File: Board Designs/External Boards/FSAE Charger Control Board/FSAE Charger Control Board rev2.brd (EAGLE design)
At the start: 67.8 x 86.5 mm, 38 parts, among them X1 CONNECTOR-4, X2 CONNECTOR-12

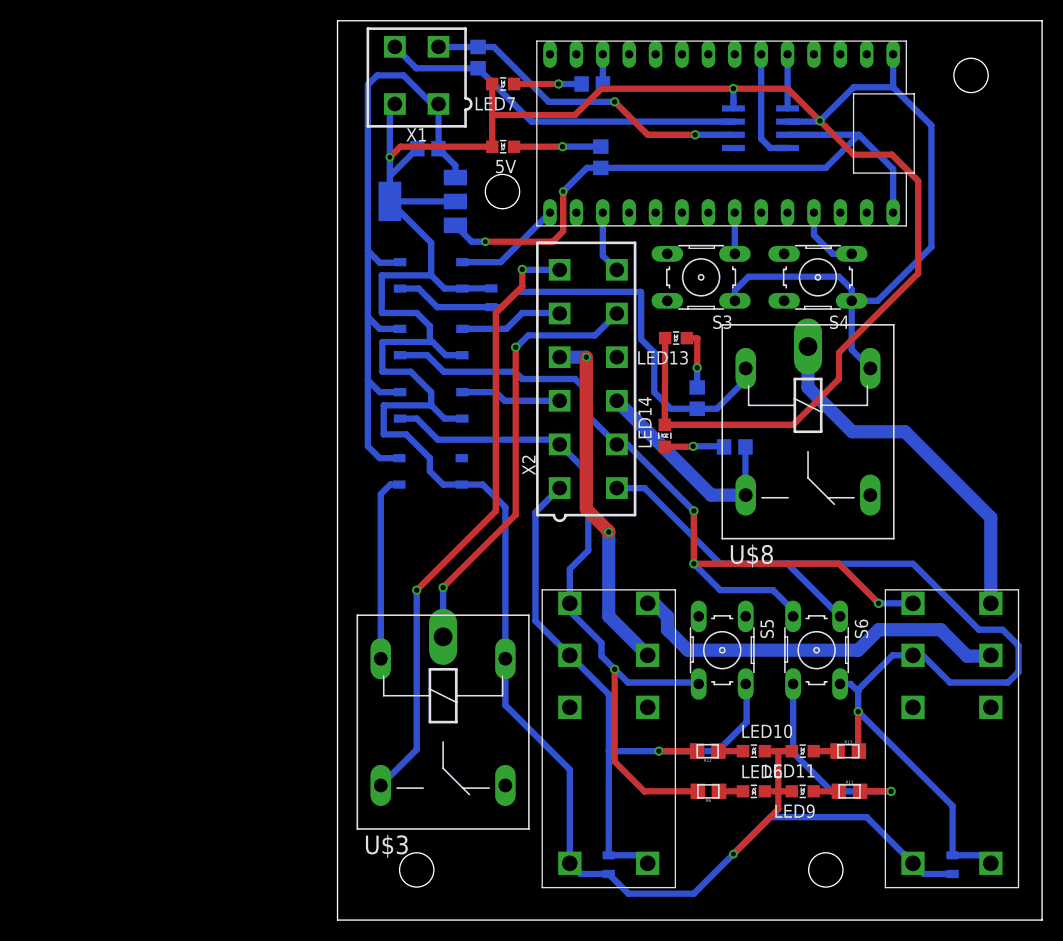
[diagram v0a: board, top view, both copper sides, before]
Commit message: Revising schematics for FSAE ESF
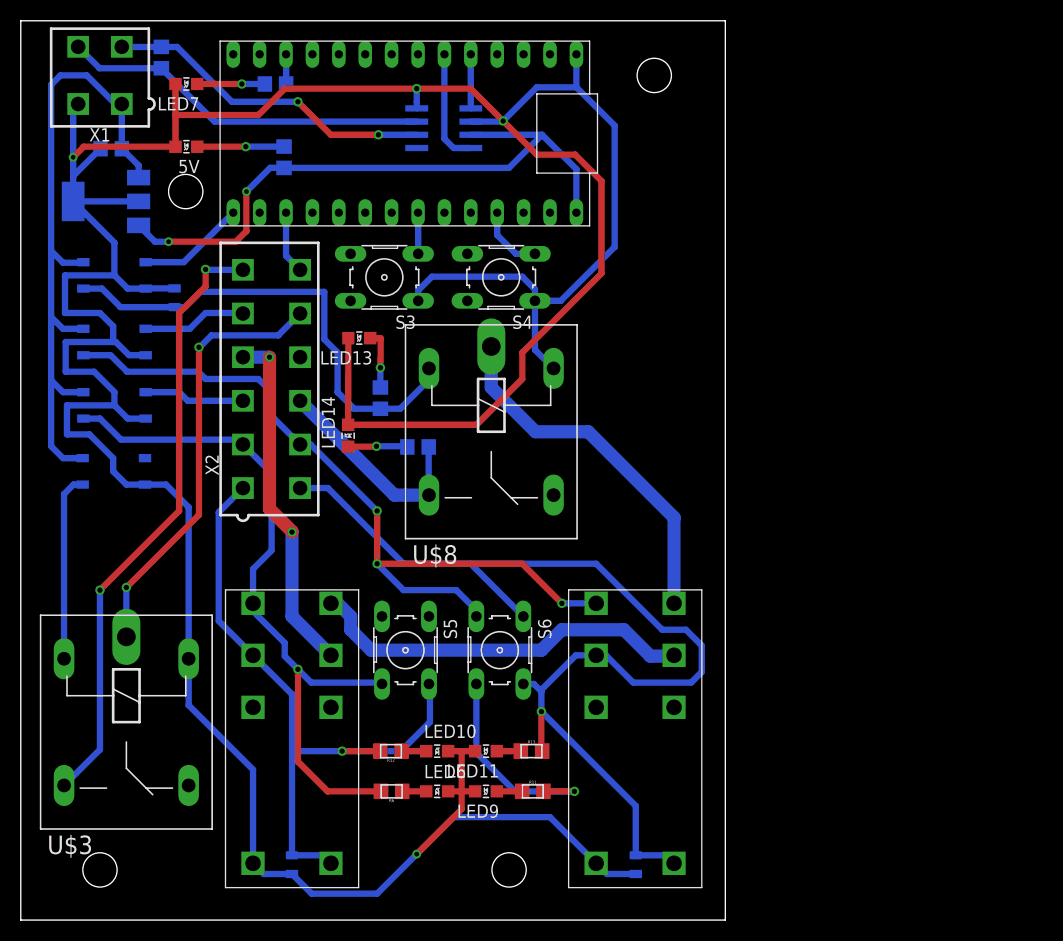
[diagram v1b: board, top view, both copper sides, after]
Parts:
- moved 5V 30.5 mm to (15.9, 74.4)
- moved 5VREG 30.5 mm to (8.19, 69.2)
- moved D5 30.5 mm to (59.2, 5.33)
- moved LED10 30.5 mm to (40.1, 16.3)
- moved LED11 30.5 mm to (44.8, 16.3)
- moved LED13 30.5 mm to (32.6, 56.0)
- moved LED6 30.5 mm to (40.1, 12.4)
- moved LED7 30.5 mm to (15.9, 80.5)
- moved LED9 30.5 mm to (44.8, 12.4)
- moved R13 30.5 mm to (49.1, 16.3)
- moved R15 30.5 mm to (34.6, 50.2)
- moved R6 30.5 mm to (35.7, 12.4)
- moved S3 30.5 mm to (35.0, 61.8)
- moved S5 30.5 mm to (37.0, 26.0)
- moved S6 30.5 mm to (46.1, 26.0)
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
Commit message: Added resistors to SSRs
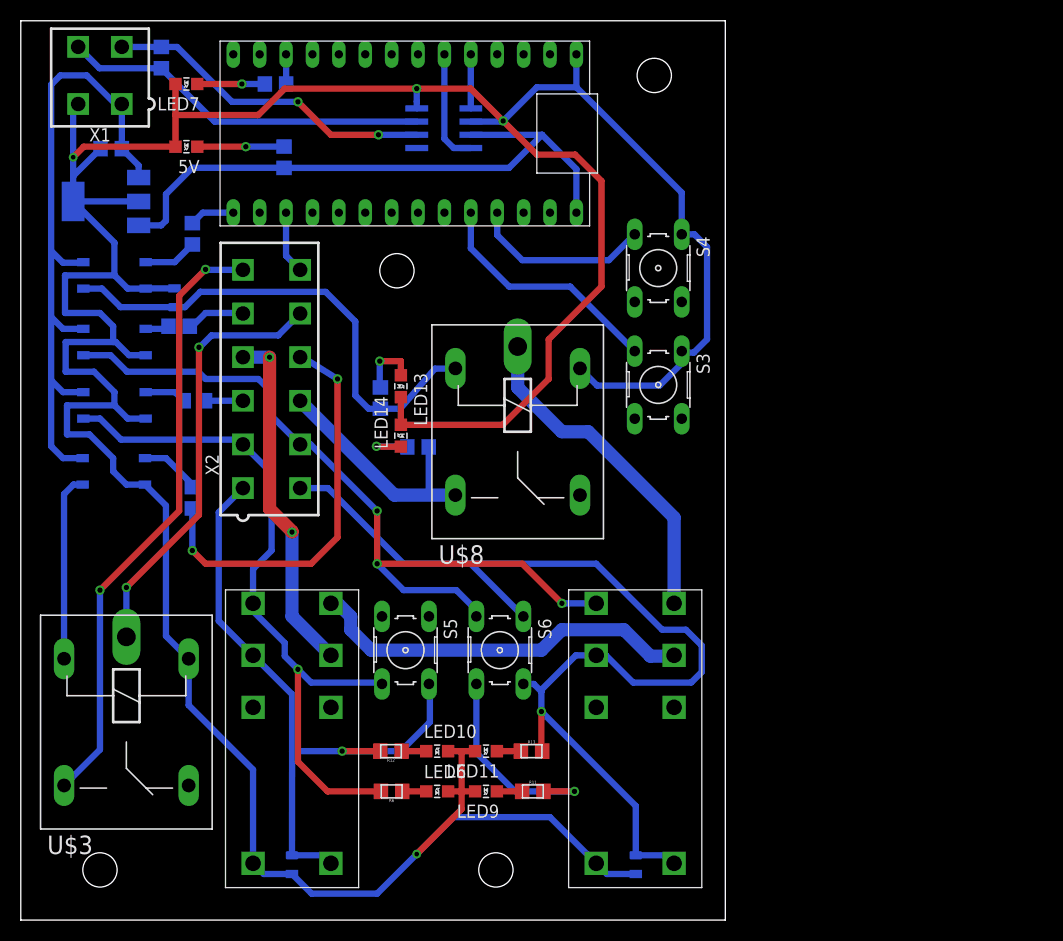
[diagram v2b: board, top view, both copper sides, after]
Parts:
- added R2, R3, R4, R5: (no value), HyTechDevices:0805
- moved S3 28.3 mm to (61.3, 51.5), turned to 270 degrees
- moved S4 15.1 mm to (61.3, 62.7), turned to 270 degrees
- moved LED13 6.12 mm to (36.6, 51.4), turned to 180 degrees
- moved LED14 5.08 mm to (36.6, 46.6)
- moved U$8 2.54 mm to (38.9, 57.1)
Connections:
- removed net BMS: BMS_SSR1.1, X2.5
- removed net IMD: IMD_SSR1.1, X2.3
- new net N$11: BMS_SSR1.1, R3.2
- new net N$15: R2.1, X2.3
- new net N$16: R3.1, X2.5
- new net N$17: R5.2, SOFT_SSR1.1
- new net N$18: R4.1, U$1.D13
- new net N$4: IMD_SSR1.1, R2.2
- net BMS_INRLK: now also R5.1, X2.10; no longer SOFT_SSR1.1
- net BTN_Y: now also U$1.A8; no longer U$1.A6
- net SW_KILL: now also R4.2; no longer U$1.D13
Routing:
- net BMS_INRLK: track 0.00 -> 39.0 mm, vias 0 -> 2
- net BTN_Y: track 3.97 -> 23.3 mm
- net GND: track 367.3 -> 354.2 mm
- net BTN_X: track 6.54 -> 17.4 mm
- net BMS: track 10.0 -> 0.00 mm
- net IMD: track 9.71 -> 0.00 mm
- net N$17: track 0.00 -> 5.85 mm
- net N$16: track 0.00 -> 5.66 mm
- net SW_KILL: track 10.4 -> 5.20 mm
- net SHUTDOWN_OUT: track 20.8 -> 25.9 mm
- net N$18: track 0.00 -> 4.35 mm
- net N$4: track 0.00 -> 4.00 mm
- net N$15: track 0.00 -> 3.66 mm
- net SHUTDOWN_IN_B: track 35.0 -> 32.4 mm
- net N$11: track 0.00 -> 2.30 mm
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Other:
- board text added: "BMS12"
- board text added: "BMSR"
- board text added: "IMD12"
- board text added: "IMDR"
- board text added: "SDOUT"
- board text added: "SWKILL"
- board text removed: "Georgia Tech HyTech Racing 2018 FSAE Charger Control Board rev2 Designed by Chad Hendrix"
- board text removed: "LED A"
- board text removed: "LED B"
- board text removed: "LED C"
- board text removed: "LED D"
